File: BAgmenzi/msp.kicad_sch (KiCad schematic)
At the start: 35 parts, among them J1 Conn_01x04, U1 MSP430FR5043IRGCT, X1 FY0800018, X2 ABS07-32.768KHZ-9-T, Y1 AWSCR-8.00CV-T

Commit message: added libraries, other changes in sch, started pcb
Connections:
- net +VCC_MAP430: no longer R1.1
- net +VCC_MSP430: now also R1.1
- net PREAMP_EN renamed VRX_EN
- net PREAMP_PWR_EN: no longer names the net of U1.26 (P1.5_TB0.5_UCB0CLK_A3_C3)
- net VGA_PWR_EN: no longer names the net of U1.19 (P1.2_UCA1SIMO_UCA1TXD_TA1.0_A8_C8)
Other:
- note added: "Debug LED: keep or drop..."
- note removed: "Debug LED"
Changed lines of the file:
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@@
 	(rectangle
 		(start 217.17 224.79)
-		(end 243.84 267.97)
+		(end 248.92 267.97)
 		(stroke
 			(width 0)
@@
 		)
 	)
-	(text "Debug LED\n"
+	(text "Debug LED: keep or drop...\n"
 		(exclude_from_sim no)
-		(at 222.758 223.774 0)
+		(at 230.378 223.52 0)
 		(effects
 			(font
@@
 	(text "Stecker muss noch ausgewählt werden.\n"
 		(exclude_from_sim no)
-		(at 336.804 58.42 0)
+		(at 334.772 71.374 0)
 		(effects
 			(font
@@
 		)
 	)
+	(text_box "use pinheaders on BREAKAWAY-> directly connect jumper cables from pin headers to MSP FET. "
+		(exclude_from_sim no)
+		(at 316.23 53.34 0)
+		(size 33.02 16.51)
+		(margins 0.9525 0.9525 0.9525 0.9525)
+		(stroke
+			(width 0)
+			(type solid)
+		)
+		(fill
+			(type color)
+			(color 249 155 255 1)
+		)
+		(effects
+			(font
+				(size 1.27 1.27)
+			)
+			(justify left top)
+		)
+	)
+	(text_box "add possibility to program through UART bootloader: \ndescribed in TI's FRAM bootloader guide, SLAU550"
+		(exclude_from_sim no)
+		(at 339.09 15.24 0)
+		(size 55.88 10.16)
+		(margins 0.9525 0.9525 0.9525 0.9525)
+		(stroke
+			(width 0)
+			(type solid)
+		)
+		(fill
+			(type color)
+			(color 249 155 255 1)
+		)
+		(effects
+			(font
+				(size 1.27 1.27)
+			)
+			(justify left top)
+		)
+	)
 	(junction
 		(at 313.69 124.46)
@@
 	(wire
 		(pts
-			(xy 36.83 50.8) (xy 40.64 50.8)
+			(xy 36.83 49.53) (xy 40.64 49.53)
 		)
 		(stroke
@@
 	(wire
 		(pts
-			(xy 90.17 60.96) (xy 92.71 60.96)
+			(xy 86.36 60.96) (xy 92.71 60.96)
 		)
 		(stroke
@@
 	(wire
 		(pts
-			(xy 43.18 68.58) (xy 36.83 68.58)
-		)
-		(stroke
-			(width 0)
-			(type default)
-		)
-	)
-	(wire
-		(pts
 			(xy 314.96 167.64) (xy 314.96 165.1)
 		)
@@
 	(wire
 		(pts
-			(xy 43.18 64.77) (xy 36.83 64.77)
-		)
-		(stroke
-			(width 0)
-			(type default)
-		)
-	)
-	(wire
-		(pts
 			(xy 238.76 139.7) (xy 234.95 139.7)
 		)
@@
 	(wire
 		(pts
+			(xy 43.18 60.96) (xy 35.56 60.96)
+		)
+		(stroke
+			(width 0)
+			(type default)
+		)
+	)
+	(wire
+		(pts
 			(xy 369.57 45.72) (xy 369.57 49.53)
 		)
@@
 	(wire
 		(pts
-			(xy 40.64 54.61) (xy 36.83 54.61)
+			(xy 40.64 53.34) (xy 36.83 53.34)
 		)
 		(stroke
@@
 	(wire
 		(pts
-			(xy 40.64 58.42) (xy 36.83 58.42)
-		)
-		(stroke
-			(width 0)
-			(type default)
-		)
-	)
-	(wire
-		(pts
 			(xy 337.82 176.53) (xy 340.36 176.53)
 		)
@@
 	)
 	(label "VGA_GAIN_RC_EN"
-		(at 40.64 54.61 0)
+		(at 40.64 53.34 0)
 		(effects
 			(font
@@
 		)
 	)
-	(label "PREAMP_PWR_EN"
-		(at 43.18 68.58 0)
-		(effects
-			(font
-				(size 1.27 1.27)
-			)
-			(justify left bottom)
-		)
-	)
 	(label "VGA_SPI.MISO"
 		(at 90.17 129.54 180)
@@
 		)
 	)
+	(label "VRX_EN"
+		(at 43.18 60.96 0)
+		(effects
+			(font
+				(size 1.27 1.27)
+			)
+			(justify left bottom)
+		)
+	)
 	(label "CH0_OUT"
 		(at 236.22 55.88 0)
@@
 	)
 	(label "VGA_GAIN_CS"
-		(at 40.64 50.8 0)
+		(at 40.64 49.53 0)
 		(effects
 			(font
@@
 		)
 	)
-	(label "PREAMP_EN"
-		(at 43.18 64.77 0)
-		(effects
-			(font
-				(size 1.27 1.27)
-			)
-			(justify left bottom)
-		)
-	)
 	(label "UUPS_TRIG_IN"
 		(at 90.17 71.12 180)
@@
 		)
 	)
-	(label "+VCC_MAP430"
+	(label "+VCC_MSP430"
 		(at 369.57 34.29 0)
 		(effects
@@
 		)
 	)
-	(label "VGA_PWR_EN"
-		(at 40.64 58.42 0)
-		(effects
-			(font
-				(size 1.27 1.27)
-			)
-			(justify left bottom)
-		)
-	)
 	(label "LINK_READY"
 		(at 43.18 140.97 0)
@@
 		)
 	)
-	(label "PREAMP_EN"
-		(at 90.17 60.96 180)
-		(effects
-			(font
-				(size 1.27 1.27)
-			)
-			(justify right bottom)
-		)
-	)
 	(label "HFXIN"
 		(at 234.95 45.72 0)
@@
 		)
 	)
-	(label "PREAMP_PWR_EN"
-		(at 90.17 66.04 180)
-		(effects
-			(font
-				(size 1.27 1.27)
-			)
-			(justify right bottom)
-		)
-	)
 	(label "DVCC1"
 		(at 355.6 167.64 0)
@@
 		)
 	)
-	(label "VGA_PWR_EN"
-		(at 90.17 58.42 180)
+	(label "VRX_EN"
+		(at 86.36 60.96 180)
 		(effects
 			(font
@@
 		)
 	)
-	(global_label "PREAMP_PWR_EN"
+	(global_label "VRX_EN"
 		(shape output)
-		(at 36.83 68.58 180)
+		(at 35.56 60.96 180)
 		(fields_autoplaced yes)
 		(effects
@@
 		)
 		(property "Intersheetrefs" "${INTERSHEET_REFS}"
-			(at 17.9397 68.58 0)
-			(effects
-				(font
-					(size 1.27 1.27)
-				)
-				(justify right)
-			)
-		)
-	)
-	(global_label "VGA_PWR_EN"
-		(shape output)
-		(at 36.83 58.42 180)
-		(fields_autoplaced yes)
-		(effects
-			(font
-				(size 1.27 1.27)
-			)
-			(justify right)
-		)
-		(property "Intersheetrefs" "${INTERSHEET_REFS}"
-			(at 21.9915 58.42 0)
+			(at 25.5596 60.96 0)
 			(effects
 				(font
@@
 	(global_label "VGA_GAIN_RC_EN"
 		(shape output)
-		(at 36.83 54.61 180)
+		(at 36.83 53.34 180)
 		(fields_autoplaced yes)
 		(effects
@@
 		)
 		(property "Intersheetrefs" "${INTERSHEET_REFS}"
-			(at 18.1814 54.61 0)
+			(at 18.1814 53.34 0)
 			(effects
 				(font
@@
 		)
 	)
-	(global_label "PREAMP_EN"
-		(shape output)
-		(at 36.83 64.77 180)
-		(fields_autoplaced yes)
-		(effects
-			(font
-				(size 1.27 1.27)
-			)
-			(justify right)
-		)
-		(property "Intersheetrefs" "${INTERSHEET_REFS}"
-			(at 22.8987 64.77 0)
-			(effects
-				(font
-					(size 1.27 1.27)
-				)
-				(justify right)
-			)
-		)
-	)
 	(global_label "SPARE_PIN"
 		(shape bidirectional)
@@
 	(global_label "VGA_GAIN_CS"
 		(shape output)
-		(at 36.83 50.8 180)
+		(at 36.83 49.53 180)
 		(fields_autoplaced yes)
 		(effects
@@
 		)
 		(property "Intersheetrefs" "${INTERSHEET_REFS}"
-			(at 21.689 50.8 0)
+			(at 21.689 49.53 0)
 			(effects
 				(font

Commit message: changed VRX rail and deleted U12
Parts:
- removed J1: Conn_01x04, symbol Connector_Generic:Conn_01x04
- removed L3, L4: 600Ohm, symbol Device:L
- added J1: Conn_01x07_MountingPin, symbol Connector_Generic_MountingPin:Conn_01x07_MountingPin
- C10, C11, C12, C13, C14, C15, C16, C17, C18, C2, C3, C4, C5, C6, C7, C8, C9: footprint (none) -> Capacitor_SMD:C_0402_1005Metric
- L1, L2: footprint (none) -> wulpus:SMD-0805
- R1, R4, R5, R6: footprint (none) -> Resistor_SMD:R_0402_1005Metric
- X2: footprint C__Users_Public_Documents_Altium_Projects_PcbLib1.PcbLib:XTAL320X150X90 -> PcbLib1:XTAL320X150X90
- Y1: footprint wulpus:AWSCR-8.00CV-T_ABR -> PcbLib1:AWSCR-8.00CV-T_ABR
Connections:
- net DVCC1 is gone; now on net DVDD_3.3: C11.2, C8.2, U1.18 (DVCC1)
- net DVCC3 is gone; now on net DVDD_3.3: C12.2, C9.2, U1.49 (DVCC3)
- net GND: now also J1.4 (Pin_4); no longer C3.1, C4.1, C5.2, C6.2, L1.2, U1.56 (PVCC), U1.57 (PVCC)
- net UUPS_TRIG_IN: no longer U1.44 (P6.5_SMCLK)
- net BSL.UART_TX: now reaches U1.21 (P2.0_UCA1CLK_UCA3SIMO_UCA3TXD)
- net BSL.UART_TX: now also J1.5 (Pin_5)
- net BSL.UART_RX: now reaches U1.22 (P2.1_UCA1STE_UCA3SOMI_UCA3RXD)
- net BSL.UART_RX: now also J1.6 (Pin_6)
- net at R6.2: now also D1.1 (C)
- net +VCC_MSP430 renamed DVDD_3.3
- net DVDD_3.3: now also J1.1 (Pin_1)
- net ADC_IN renamed SIG_FILT_IN
- net JTAG_RESET_N renamed JTAG.RESET_N
- net JTAG.RESET_N: now also J1.3 (Pin_3)
- net JTAG_TEST renamed JTAG.TEST
- net JTAG.TEST: now also J1.2 (Pin_2)
- net NRF_DATA_READY renamed DATA_READY
- net NRF_LINK_READY renamed LINK_READY
- net NRF_SPI.CLK renamed NRF_SPI.SCLK
- net PULSER_OUT renamed PULSE_OUT
- new net PVCC: C3.1, C4.1, C5.2, C6.2, L1.2, U1.56 (PVCC), U1.57 (PVCC)
- no-connect marks 0 -> 1
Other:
- moved on the sheet: C1, C10, C11, C12, C3, C4, C5, C6, C7, C8, C9, L1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

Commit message: started layout, front v backside
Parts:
- removed D1: APHD1608LZGCK, wulpus:FP-APHD1608LZGCK-MFG, symbol wulpus:CMP-44529-000045-1
- removed J1: Conn_01x07_MountingPin, symbol Connector_Generic_MountingPin:Conn_01x07_MountingPin
- removed R6: 22, Resistor_SMD:R_0402_1005Metric, symbol Device:R
- removed TP1: TestPoint, symbol Connector:TestPoint
- added J1: Conn_01x07, Connector_PinHeader_2.54mm:PinHeader_1x07_P2.54mm_Vertical, symbol Connector_Generic:Conn_01x07
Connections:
- net BSL.UART_RX: now also J1.6 (Pin_6)
- net BSL.UART_TX: now also J1.5 (Pin_5)
- net DVDD_3.3: now also J1.1 (Pin_1)
- net GND: now also J1.4 (Pin_4)
- net JTAG.RESET_N: now also J1.3 (Pin_3)
- net JTAG.TEST: now also J1.2 (Pin_2)
- net TRIG_OUT: no longer names the net of U1.45 (P6.6_ACLK)
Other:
- note removed: "Debug LED: keep or drop..."

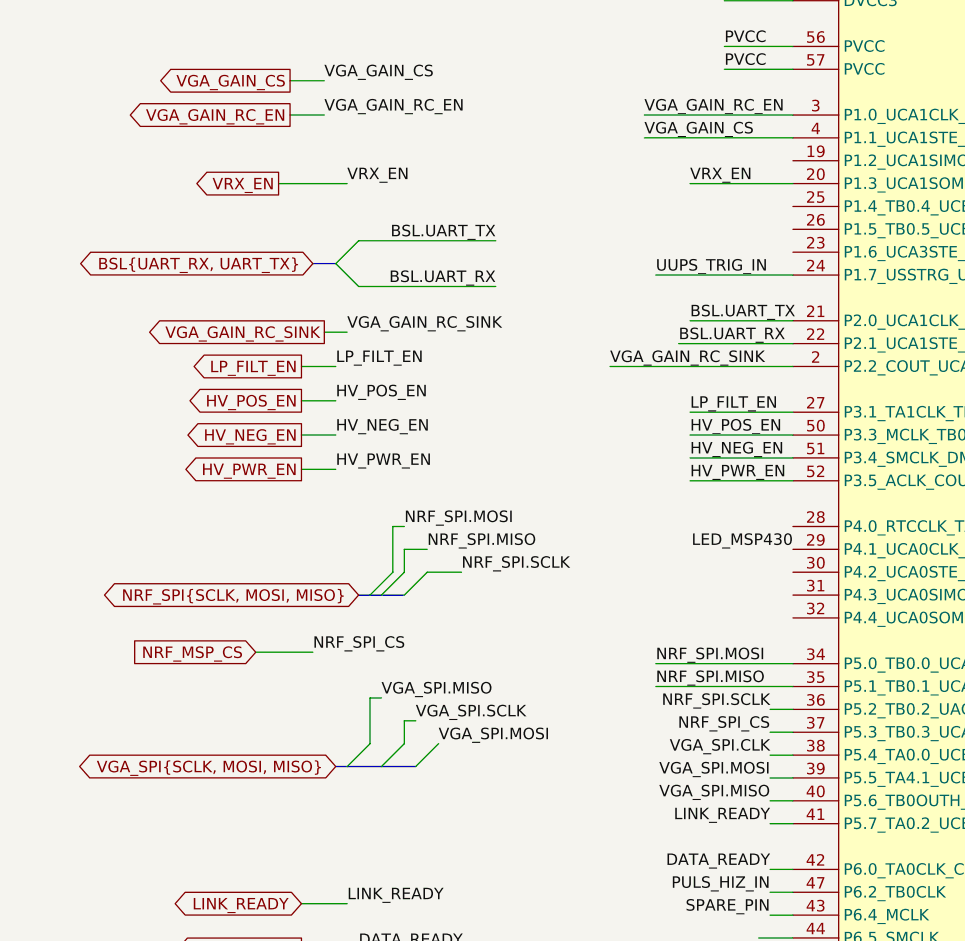
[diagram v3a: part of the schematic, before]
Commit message: started routing, changed enable signals to nRF
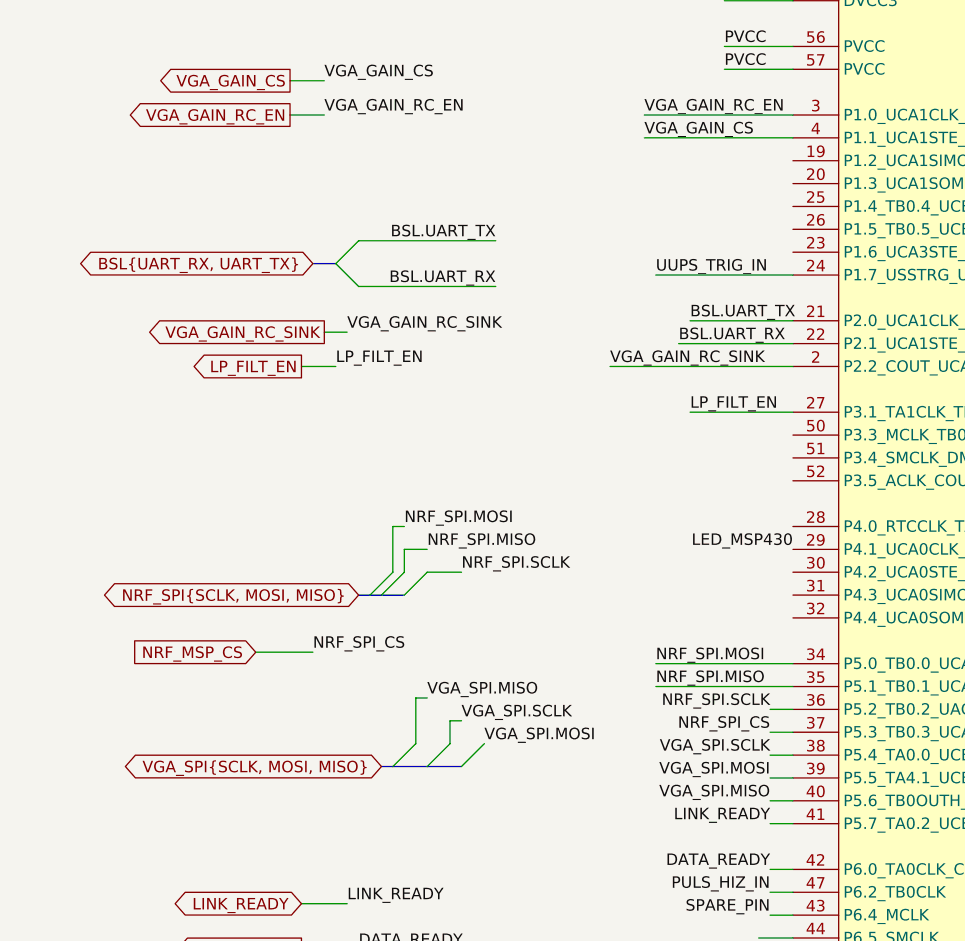
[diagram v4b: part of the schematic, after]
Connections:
- net VGA_SPI.CLK is gone; now on net VGA_SPI.SCLK: U1.38 (P5.4_TA0.0_UCB1CLK_TA4.0)
- net HV_NEG_EN: no longer names the net of U1.51 (P3.4_SMCLK_DMAE0)
- net HV_POS_EN: no longer names the net of U1.50 (P3.3_MCLK_TB0.3_XPB1)
- net HV_PWR_EN: no longer names the net of U1.52 (P3.5_ACLK_COUT)
- net VRX_EN: no longer names the net of U1.20 (P1.3_UCA1SOMI_UCA1RXD_TA1.1_A9_C9)

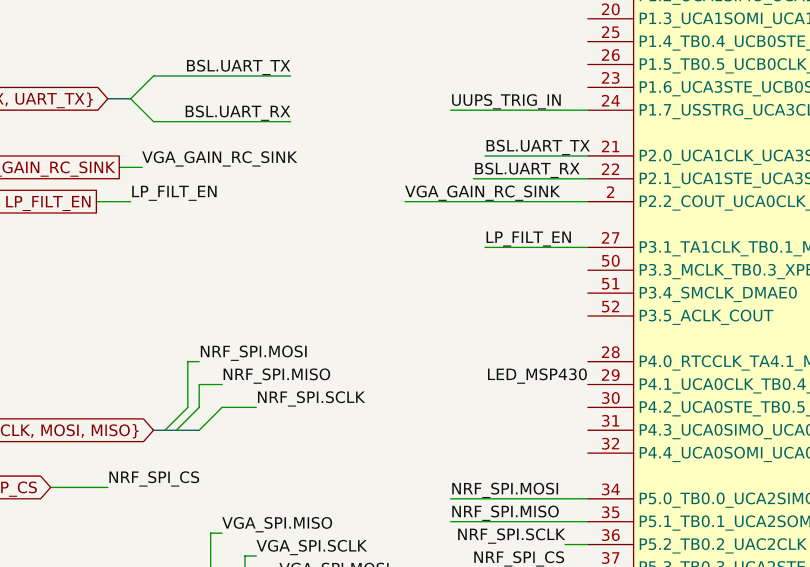
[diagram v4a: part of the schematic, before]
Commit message: routed msp and nrf
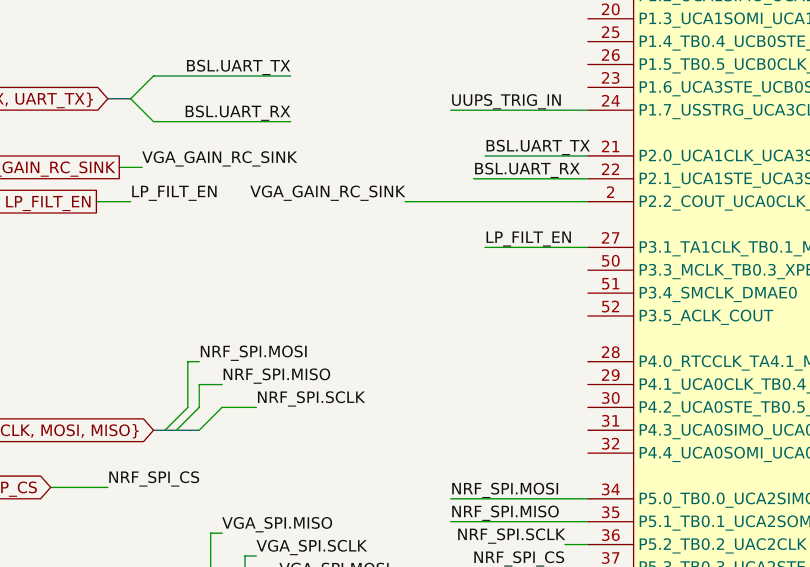
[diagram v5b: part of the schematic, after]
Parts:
- C1: footprint (none) -> Capacitor_SMD:C_0402_1005Metric
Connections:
- net LED_MSP430: no longer names the net of U1.29 (P4.1_UCA0CLK_TB0.4_UCA3SOMI_UCA3RXD)
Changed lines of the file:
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@@
 		)
 	)
-	(label "LED_MSP430"
-		(at 92.71 101.6 180)
-		(effects
-			(font
-				(size 1.27 1.27)
-			)
-			(justify right bottom)
-		)
-	)
 	(label "USSXTIN"
 		(at 234.95 68.58 0)
@@
 	)
 	(label "VGA_GAIN_RC_SINK"
-		(at 72.39 81.28 0)
+		(at 72.39 81.28 180)
 		(effects
 			(font
 				(size 1.27 1.27)
 			)
-			(justify left bottom)
+			(justify right bottom)
 		)
 	)
@@
 			)
 		)
-		(property "Footprint" ""
+		(property "Footprint" "Capacitor_SMD:C_0402_1005Metric"
 			(at 257.81 52.3748 0)
 			(effects

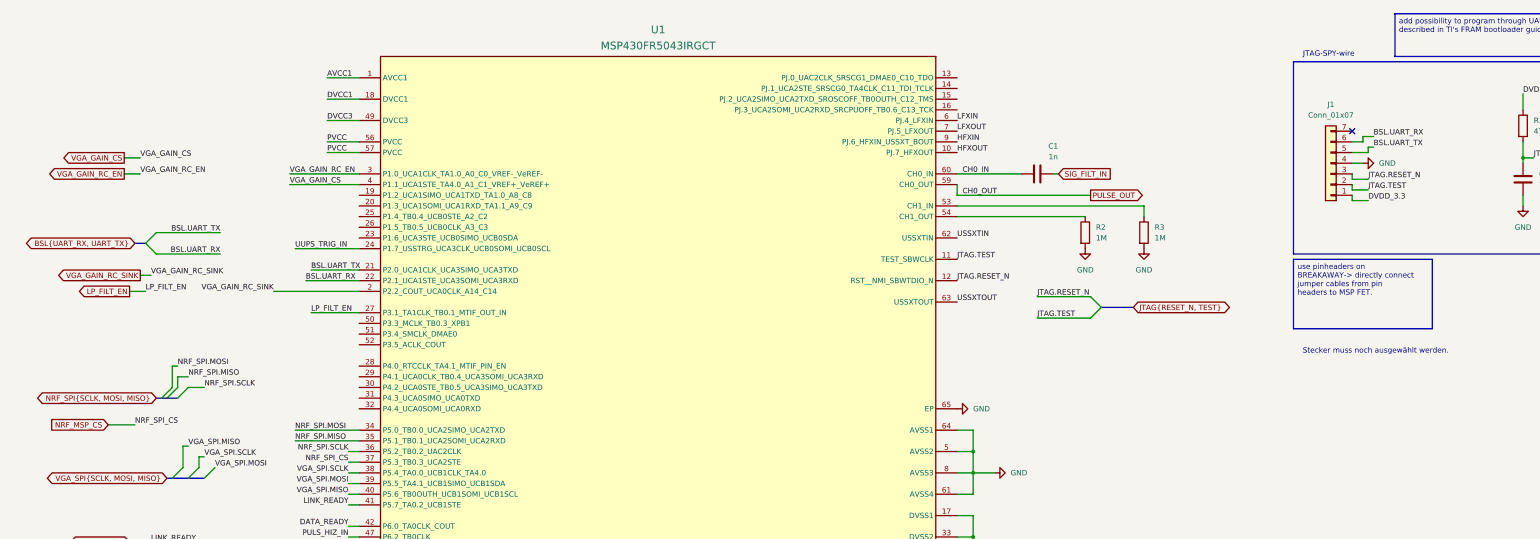
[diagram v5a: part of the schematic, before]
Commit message: added polyCMUT footprint, changed enables, more compact
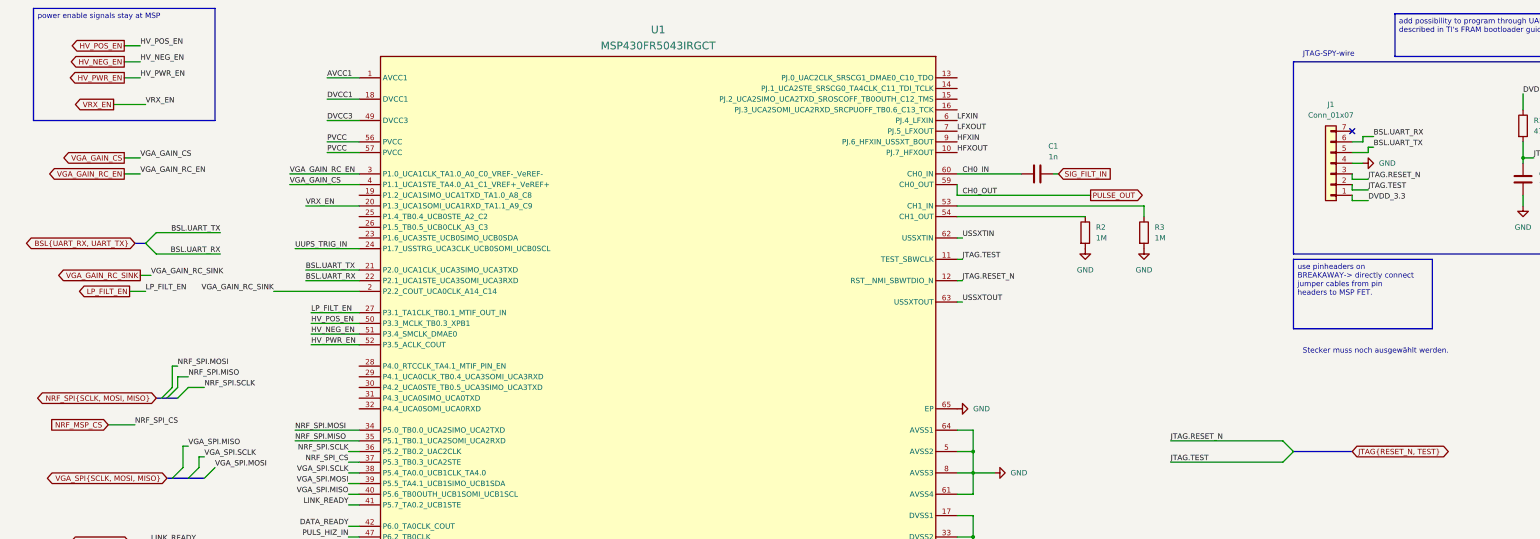
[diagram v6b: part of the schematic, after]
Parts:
- R2, R3: footprint (none) -> Resistor_SMD:R_0402_1005Metric
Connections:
- net VRX_EN: now reaches U1.20 (P1.3_UCA1SOMI_UCA1RXD_TA1.1_A9_C9)
- net HV_POS_EN: now reaches U1.50 (P3.3_MCLK_TB0.3_XPB1)
- net HV_NEG_EN: now reaches U1.51 (P3.4_SMCLK_DMAE0)
- net HV_PWR_EN: now reaches U1.52 (P3.5_ACLK_COUT)

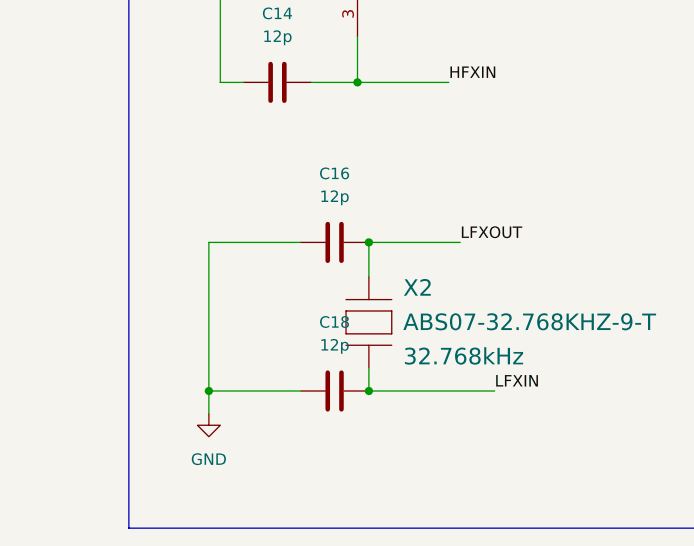
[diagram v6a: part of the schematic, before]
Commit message: part numbers added
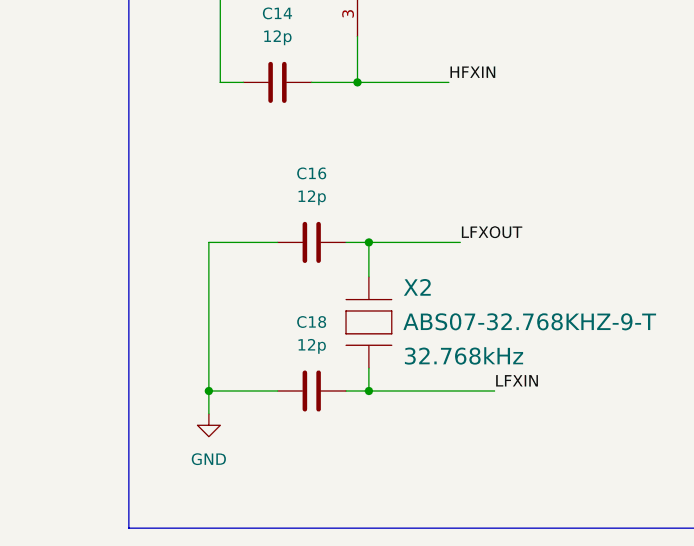
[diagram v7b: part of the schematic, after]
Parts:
- C1, C2, C5, C6: LCSC Part # (none) -> C3832658
- C10, C11, C12, R4, R5: LCSC Part # (none) -> C161362
- C13, C14, C15, C16, C17, C18: LCSC Part # (none) -> C2176190
- C3, C4: footprint Capacitor_SMD:C_0402_1005Metric -> Capacitor_SMD:C_0603_1608Metric
- C7, C8, C9: LCSC Part # (none) -> C12530
- L1, L2: LCSC Part # (none) -> C2661857
- R1: LCSC Part # (none) -> C880417
- R2, R3: LCSC Part # (none) -> C473625
- U1: LCSC Part # (none) -> C3189129
- X1: LCSC Part # (none) -> C6951614
- X2: LCSC Part # (none) -> C179635
- Y1: LCSC Part # (none) -> C2650764
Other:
- moved on the sheet: C16, C18
